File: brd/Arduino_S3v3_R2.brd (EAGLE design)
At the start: 62.2 x 49.2 mm, 35 parts, among them J2 PORT C(A0-A5), J4 USB_B_PTH, U1 FT232RL, U2 ATMEGA328P_TQFP, Y1 16MHz

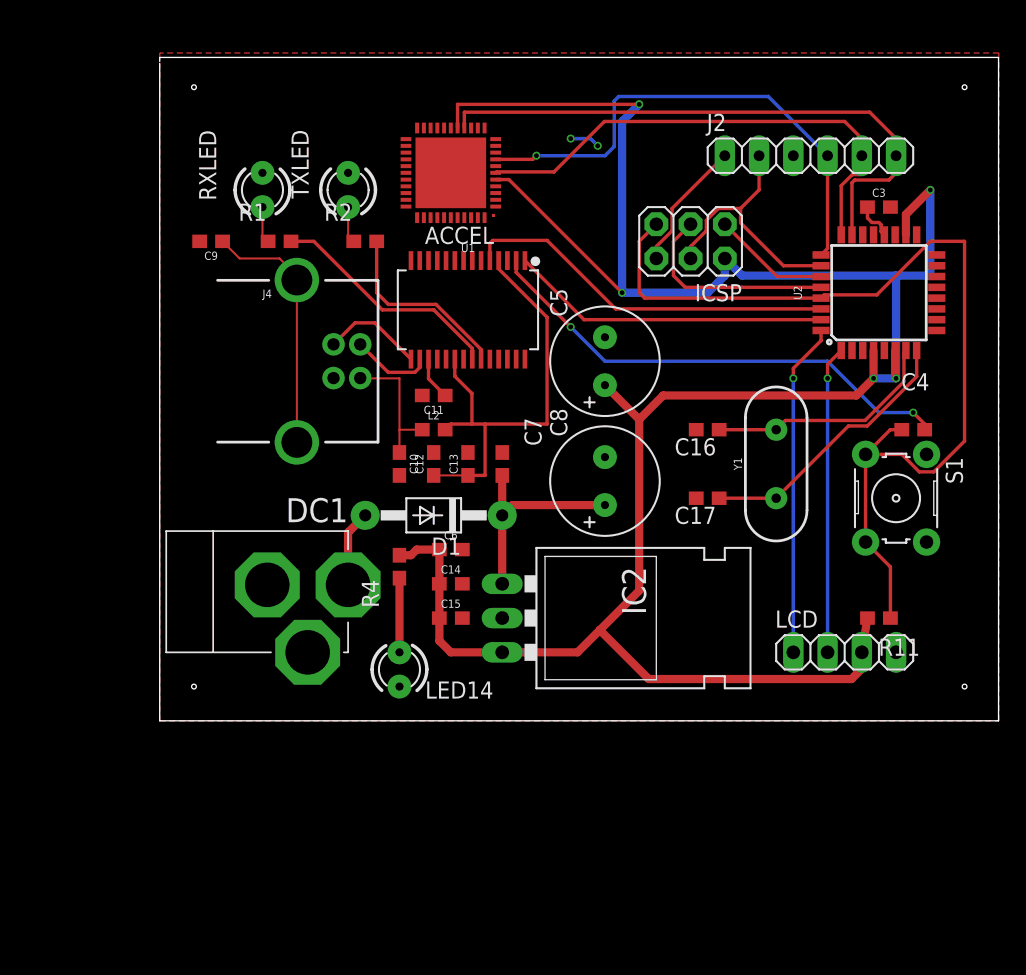
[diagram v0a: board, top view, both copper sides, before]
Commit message: Added buzzer, adjusted for SPI, new accel, pot in
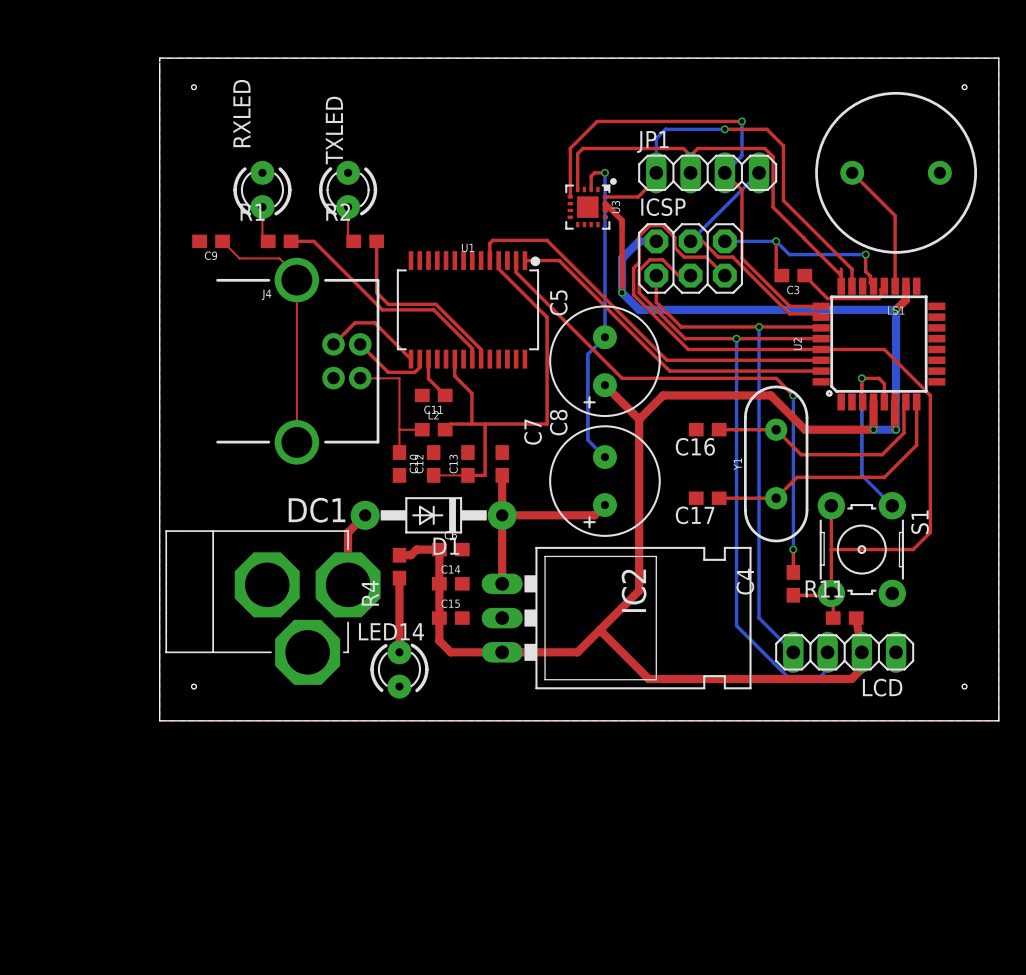
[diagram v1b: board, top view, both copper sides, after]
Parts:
- removed ACCEL: LIS3L02AQ3, st-microelectronics:QFN-44-7X7
- removed J2: PORT C(A0-A5), pinhead:1X06
- added JP1: (no value), pinhead:1X04
- added LS1: BUZZER-PTH, SparkFun-Electromechanical:BUZZER-12MM
- added U3: ADXL337, SparkFun-Sensors:LFCSP-16-3X3
- LED14: value POWER LED -> POWER
- moved C4 14.5 mm to (47.0, 10.2), turned to 90 degrees
- moved C3 8.13 mm to (47.0, 33.0), turned to 180 degrees
- moved S1 4.58 mm to (52.1, 12.7)
- moved U2 3.81 mm to (53.3, 27.9)
- moved R11 2.54 mm to (50.8, 7.62), turned to 0 degrees
- moved ICSP 1.27 mm to (39.4, 34.3), turned to 0 degrees
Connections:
- net N$35 renamed RXLED
- net N$36 renamed TXLED
- net N$49 renamed RXD
- net N$50 renamed TXD
- removed net N$1: LCD.2, U2.1
- removed net N$10: ACCEL.15, J2.6, U2.23
- removed net N$11: ACCEL.6, J2.5, U2.24
- removed net N$12: ACCEL.8, J2.4, U2.25
- removed net N$51: LCD.1, U2.32
- removed net SPKP: ICSP.4, J2.2, U2.26
- new net BUZZ: LS1.+, U2.19
- new net POTIN: ICSP.4, JP1.4, U2.26
- new net XOUT: JP1.3, U2.25, U3.5
- new net YOUT: JP1.2, U2.24, U3.4
- new net ZOUT: JP1.1, U2.23, U3.16
- net +5V: now also U3.14, U3.15; no longer ACCEL.16, ACCEL.5
- net GND: now also LS1.-, U3.2, U3.6, U3.7; no longer ACCEL.14, ACCEL.4, ACCEL.7, J2.1
- net N$14: now also LCD.1
- net N$15: now also LCD.2
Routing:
- net N$10: track 44.0 -> 0.00 mm
- net GND: track 12.0 -> 55.7 mm, vias 2 -> 4
- net +5V: track 178.6 -> 138.3 mm, vias 5 -> 4
- net N$12: track 37.9 -> 0.00 mm, vias 1 -> 0
- net N$11: track 37.4 -> 0.00 mm
- net N$15: track 15.6 -> 52.3 mm, vias 0 -> 1
- net XOUT: track 0.00 -> 35.7 mm, vias 0 -> 1
- net YOUT: track 0.00 -> 31.4 mm
- net N$14: track 8.74 -> 40.2 mm, vias 0 -> 1
- net ZOUT: track 0.00 -> 30.1 mm, vias 0 -> 1
- net N$51: track 24.7 -> 0.00 mm, vias 1 -> 0
- net N$1: track 22.8 -> 0.00 mm, vias 1 -> 0
- net POTIN: track 0.00 -> 19.2 mm
- net SPKP: track 19.0 -> 0.00 mm
- net BUZZ: track 0.00 -> 9.72 mm
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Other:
- board size 62.2 x 49.2 mm -> 62.2 x 49.1 mm

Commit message: Board design final dimensions. Rough Draft ready.
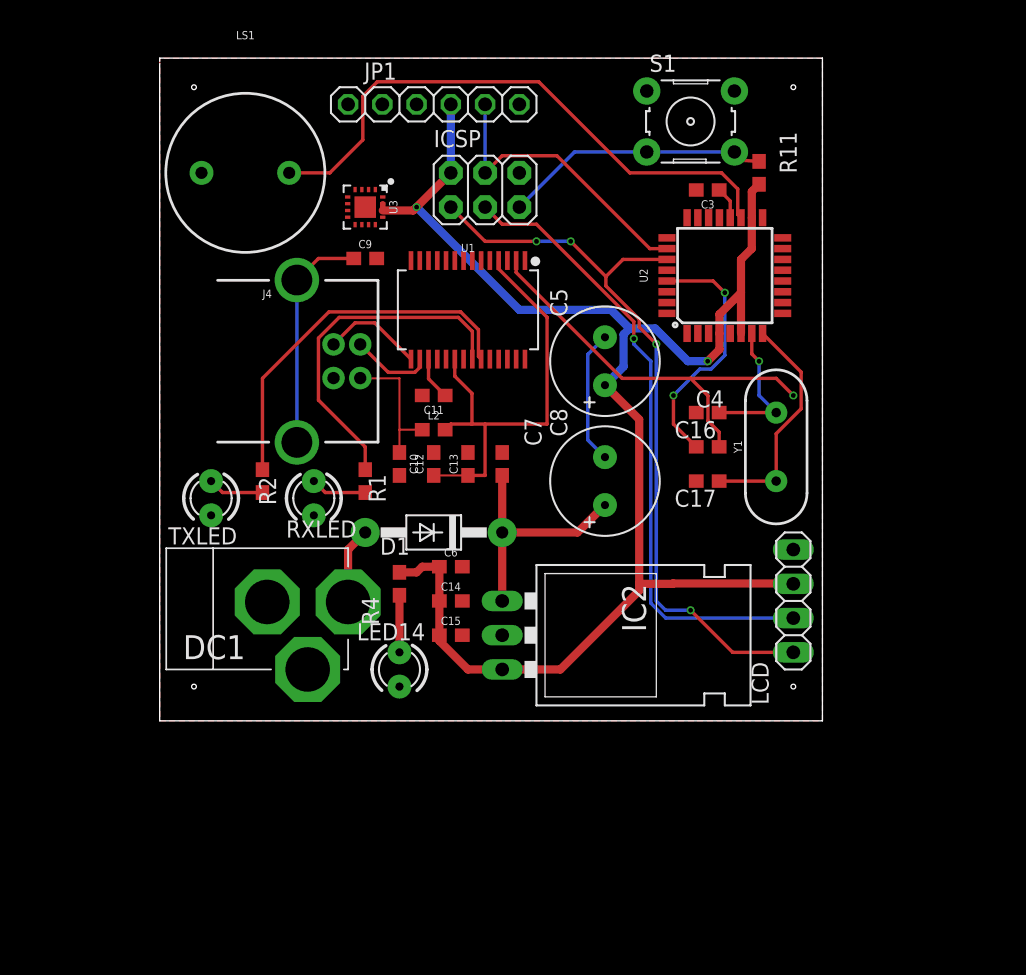
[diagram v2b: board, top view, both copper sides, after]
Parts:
- JP1: device pinhead:1X04 -> adafruit:1X06
- moved LS1 48.3 mm to (6.35, 40.6), turned to 0 degrees
- moved S1 34.2 mm to (39.4, 44.5), turned to 0 degrees
- moved R11 33.6 mm to (44.5, 40.6), turned to 270 degrees
- moved TXLED 25.0 mm to (3.81, 16.5), turned to 270 degrees
- moved RXLED 23.2 mm to (11.4, 16.5), turned to 270 degrees
- moved JP1 20.9 mm to (20.3, 45.7)
- moved R2 19.3 mm to (7.62, 17.8), turned to 90 degrees
- moved R1 18.9 mm to (15.2, 17.8), turned to 90 degrees
- moved U3 16.5 mm to (15.2, 38.1)
- moved ICSP 16.1 mm to (24.1, 39.4)
- moved U2 12.5 mm to (41.9, 33.0)
- moved C4 12.0 mm to (40.6, 20.3), turned to 0 degrees
- moved C9 11.5 mm to (15.2, 34.3), turned to 0 degrees
- moved C3 8.98 mm to (40.6, 39.4)
- moved LCD 5.39 mm to (47.0, 8.89), turned to 90 degrees
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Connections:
- net +5V: now also JP1.4
- net GND: now also JP1.6
- net POTIN: now also JP1.5; no longer JP1.4
- net XOUT: now also U3.16; no longer U3.5
- net ZOUT: now also U3.5; no longer U3.16
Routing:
- net GND: track 55.7 -> 10.4 mm, vias 4 -> 0
- net XOUT: track 35.7 -> 0.00 mm, vias 1 -> 0
- net BUZZ: track 9.72 -> 43.5 mm
- net YOUT: track 31.4 -> 0.00 mm
- net ZOUT: track 30.1 -> 0.00 mm, vias 1 -> 0
- net RXD: track 29.6 -> 0.45 mm
- net RESET: track 67.6 -> 38.9 mm, vias 0 -> 2
- net TXD: track 25.4 -> 0.00 mm
- net +5V: track 138.3 -> 115.3 mm, vias 4 -> 2
- net N$14: track 40.2 -> 56.0 mm, vias 1 -> 4
- net TXLED: track 14.0 -> 27.6 mm
- net RXLED: track 17.5 -> 25.7 mm
- net N$4: track 38.3 -> 31.2 mm, vias 2 -> 1
- net N$7: track 17.5 -> 10.8 mm, vias 0 -> 1
- net N$15: track 52.3 -> 47.0 mm
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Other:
- board size 62.2 x 49.1 mm -> 49.1 x 49.1 mm

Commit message: Thickened lines for board outline to width 5
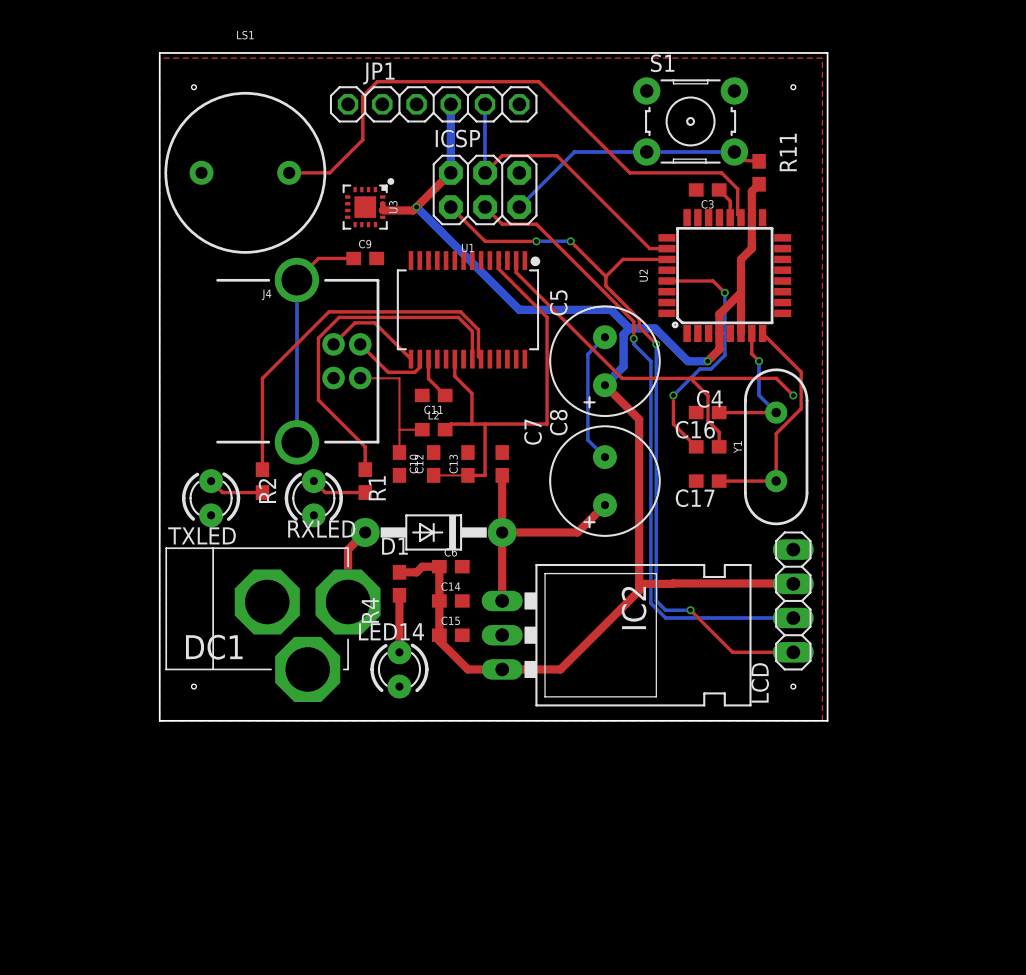
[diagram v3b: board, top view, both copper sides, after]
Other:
- board size 49.1 x 49.1 mm -> 49.5 x 49.5 mm
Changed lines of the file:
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@@
 <?xml version="1.0" encoding="utf-8"?>
 <!DOCTYPE eagle SYSTEM "eagle.dtd">
-<eagle version="9.4.2">
+<eagle version="9.6.2">
 <drawing>
 <settings>
@@
 <board>
 <plain>
-<wire x1="0" y1="0" x2="49.149" y2="0" width="0" layer="20"/>
-<wire x1="49.149" y1="0" x2="49.149" y2="49.149" width="0" layer="20"/>
-<wire x1="49.149" y1="49.149" x2="0" y2="49.149" width="0" layer="20"/>
-<wire x1="0" y1="49.149" x2="0" y2="48.905509375" width="0" layer="20"/>
-<wire x1="0" y1="48.753109375" x2="0" y2="0" width="0" layer="20"/>
 <hole x="2.54" y="2.54" drill="0.35"/>
 <hole x="2.54" y="46.99" drill="0.35"/>
@@
 <dimension x1="0" y1="0" x2="0" y2="49.149" x3="-8.89" y3="24.5745" textsize="1.778" layer="1"/>
 <dimension x1="0" y1="0" x2="49.149" y2="0" x3="24.5745" y3="-3.81" textsize="1.778" layer="1"/>
+<wire x1="0" y1="49.53" x2="0" y2="0" width="0.127" layer="20"/>
+<wire x1="0" y1="0" x2="49.53" y2="0" width="0.127" layer="20"/>
+<wire x1="49.53" y1="0" x2="49.53" y2="49.53" width="0.127" layer="20"/>
+<wire x1="49.53" y1="49.53" x2="0" y2="49.53" width="0.127" layer="20"/>
 </plain>
 <attributes>

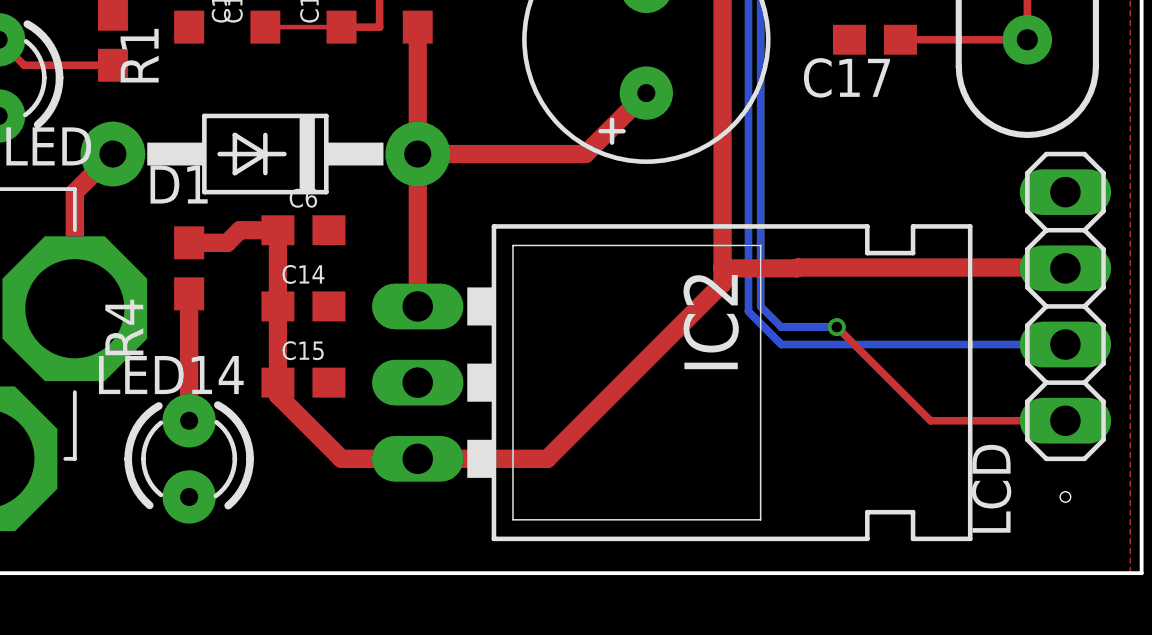
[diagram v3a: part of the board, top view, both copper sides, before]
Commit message: Added initial manufacturing part numbers
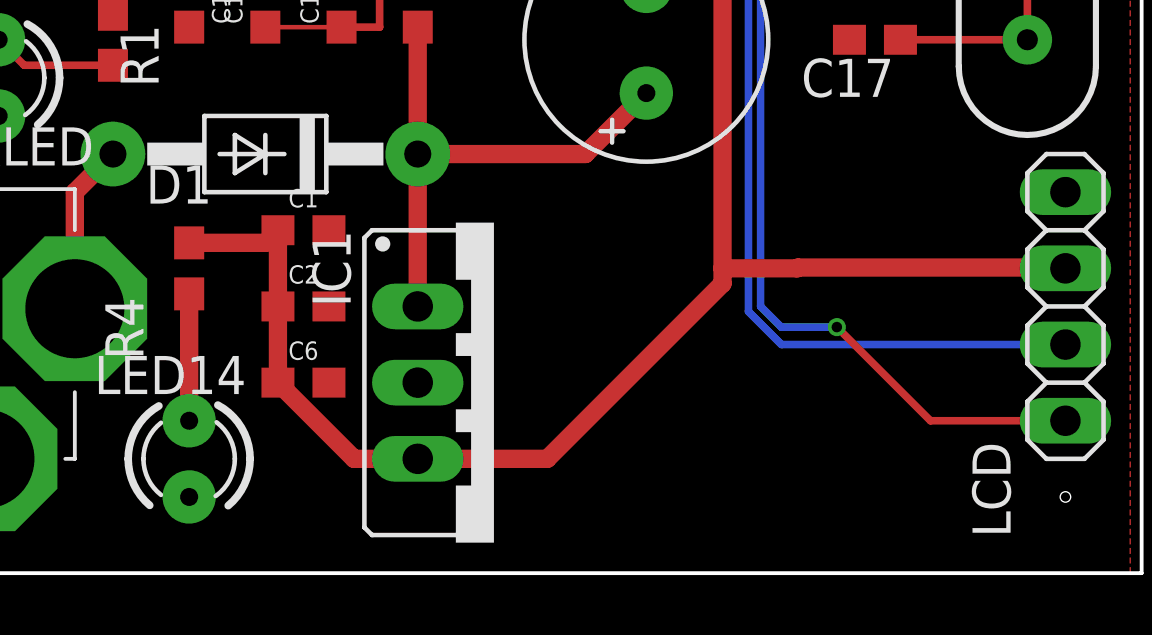
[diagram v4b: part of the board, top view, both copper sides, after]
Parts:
- removed C15: 0.1uF, SparkFun-Capacitors:0603
- removed IC2: (no value), v-reg:78XXL
- added C1: 0.1uF, SparkFun-Capacitors:0603
- added IC1: (no value), v-reg:78XXS
- moved C6 5.08 mm to (21.6, 6.35)
- renumbered C14 to C2
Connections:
- net +5V: now also C1.1, IC1.OUT; no longer C15.1, IC2.OUT
- net GND: now also C1.2, IC1.GND; no longer C15.2, IC2.GND
- net VIN: now also IC1.IN; no longer IC2.IN

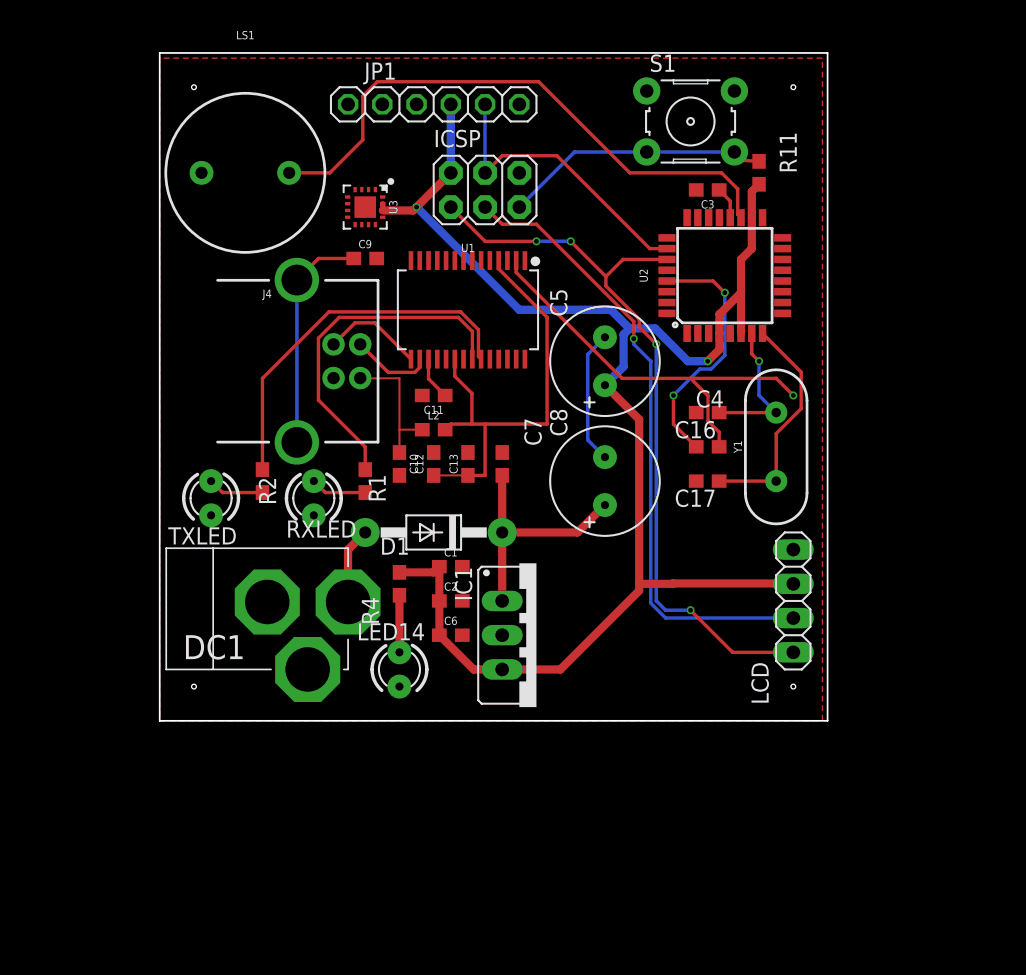
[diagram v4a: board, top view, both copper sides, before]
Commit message: updated to SPI, replaced TH comps, new accel
New accelerometer is not hooked up yet.
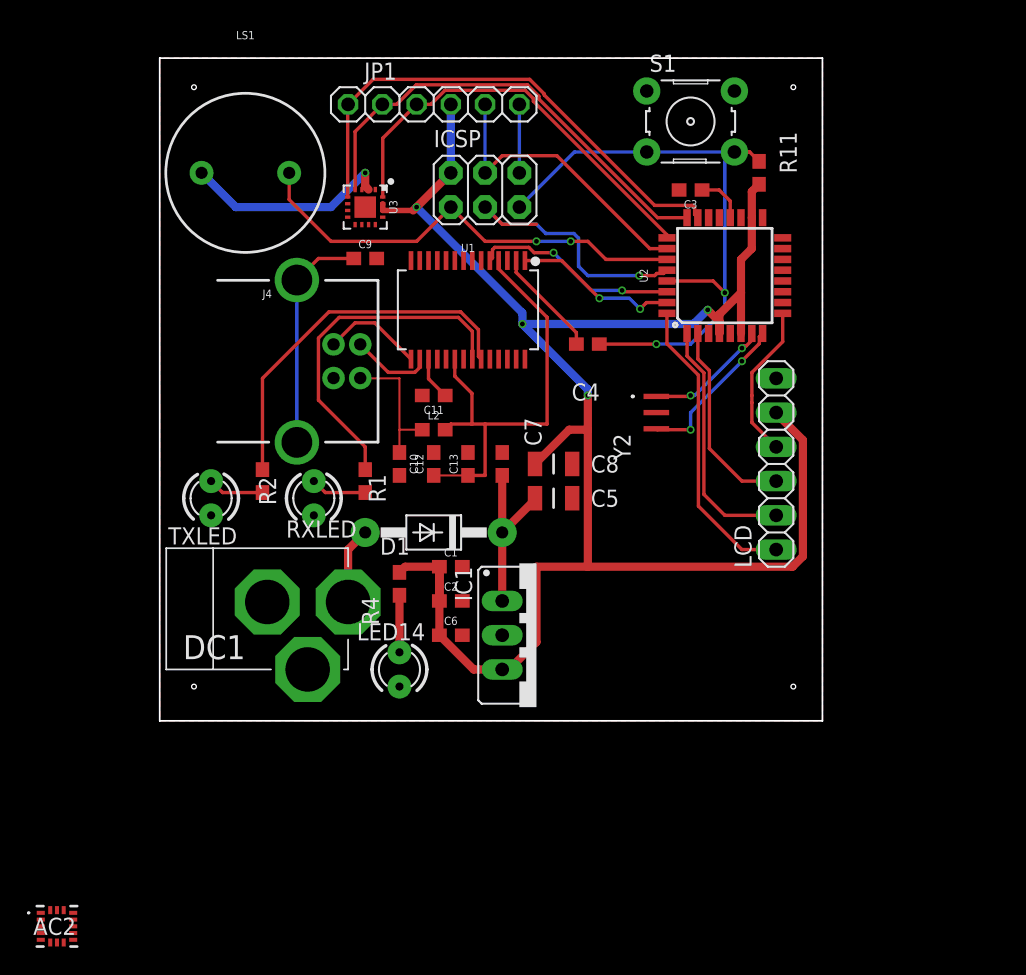
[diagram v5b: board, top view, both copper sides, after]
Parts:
- removed C16, C17: 30p, rcl:C0603
- removed Y1: 16MHz, SparkFun-Clocks:HC49US
- added AC2: LIS3DHTR, SamacSys_Parts:LIS3DHTR
- added Y2: CSTNE16M0V51Z000R0, SamacSys_Parts:CSTNE16M0V51Z000R0
- C5, C8: value 100u -> GRM31CR61A107ME05L; device rcl:E3,5-8 -> SamacSys_Parts:CAPC3216X180N
- LCD: device pinhead:1X04 -> pinhead:1X06
- moved C4 11.7 mm to (31.8, 27.9), turned to 180 degrees
- moved C5 10.9 mm to (29.2, 16.5), turned to 0 degrees
- moved LCD 10.2 mm to (45.7, 19.1)
- moved C8 4.02 mm to (29.2, 19.1), turned to 0 degrees
- moved C3 1.27 mm to (39.4, 39.4)
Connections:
- removed net N$14: ICSP.1, LCD.1, U2.27
- removed net N$7: C16.1, U2.7, Y1.2
- new net GND_1: AC2.5
- new net GND_2: AC2.12
- new net LCD_CS: LCD.1, U2.32
- new net LCD_SCL: LCD.4, U2.9
- new net LCD_SDA: LCD.3, U2.2
- new net LCD_SDO: LCD.2, U2.1
- new net N$1: U2.7, Y2.1
- new net VDD: AC2.14
- new net VDDIO: AC2.1
- net +5V: now also C8.1, LCD.5; no longer C5.+, LCD.3
- net BUZZ: now also ICSP.1, U2.27; no longer U2.19
- net GND: now also C5.2, C8.2, LCD.6, Y2.2; no longer C16.2, C17.2, C5.-, C8.-, LCD.4
- net N$15: no longer LCD.2
- net N$6: now also Y2.3; no longer C17.1, Y1.1
- net VIN: now also C5.1; no longer C8.+
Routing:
- net N$14: track 56.0 -> 0.00 mm, vias 4 -> 0
- net ZOUT: track 0.00 -> 38.2 mm
- net YOUT: track 0.00 -> 34.6 mm
- net XOUT: track 0.00 -> 31.7 mm
- net N$15: track 47.0 -> 21.3 mm
- net N$4: track 31.2 -> 8.26 mm, vias 1 -> 0
- net LCD_CS: track 0.00 -> 22.4 mm
- net +5V: track 115.0 -> 137.2 mm, vias 2 -> 4
- net LCD_SDO: track 0.00 -> 18.5 mm
- net LCD_SDA: track 0.00 -> 14.8 mm
- net RXD: track 0.45 -> 15.3 mm, vias 0 -> 2
- net TXD: track 0.00 -> 12.2 mm, vias 0 -> 2
- net LCD_SCL: track 0.00 -> 11.6 mm
- net N$7: track 10.8 -> 0.00 mm, vias 1 -> 0
- net GND: track 10.4 -> 21.2 mm, vias 0 -> 1
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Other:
- board size 49.5 x 49.5 mm -> 49.1 x 49.1 mm
